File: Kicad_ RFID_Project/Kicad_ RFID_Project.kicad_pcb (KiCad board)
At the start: 2 copper layers, 75 x 75 mm, 34 parts, among them J1 Conn_01x08, J2 Conn_ST_STDC14, J3 10172013-00011LF, Q1 2N3904, SW1 RESET, U1 STM32L476RGTx, U2 AZ1117CH2-3.3

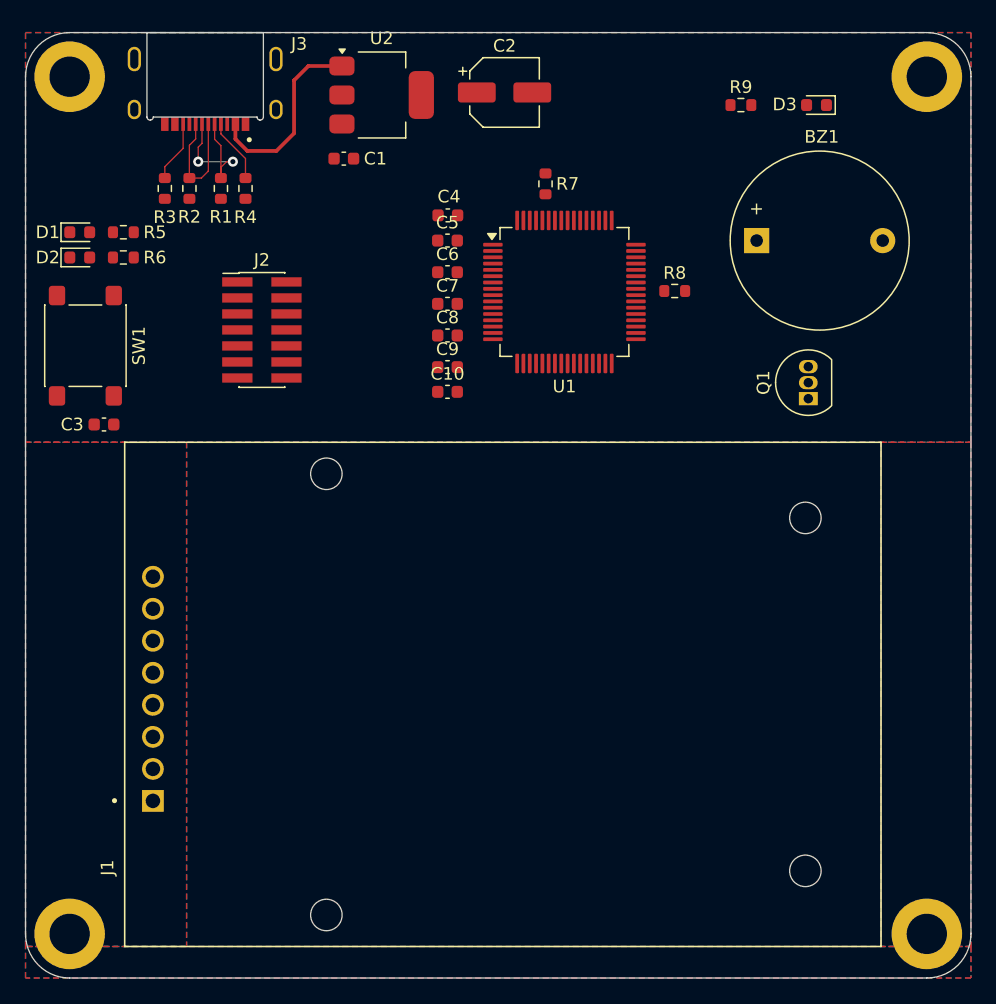
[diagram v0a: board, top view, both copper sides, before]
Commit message: ajout des leds electrostatiques pour l'USB-C
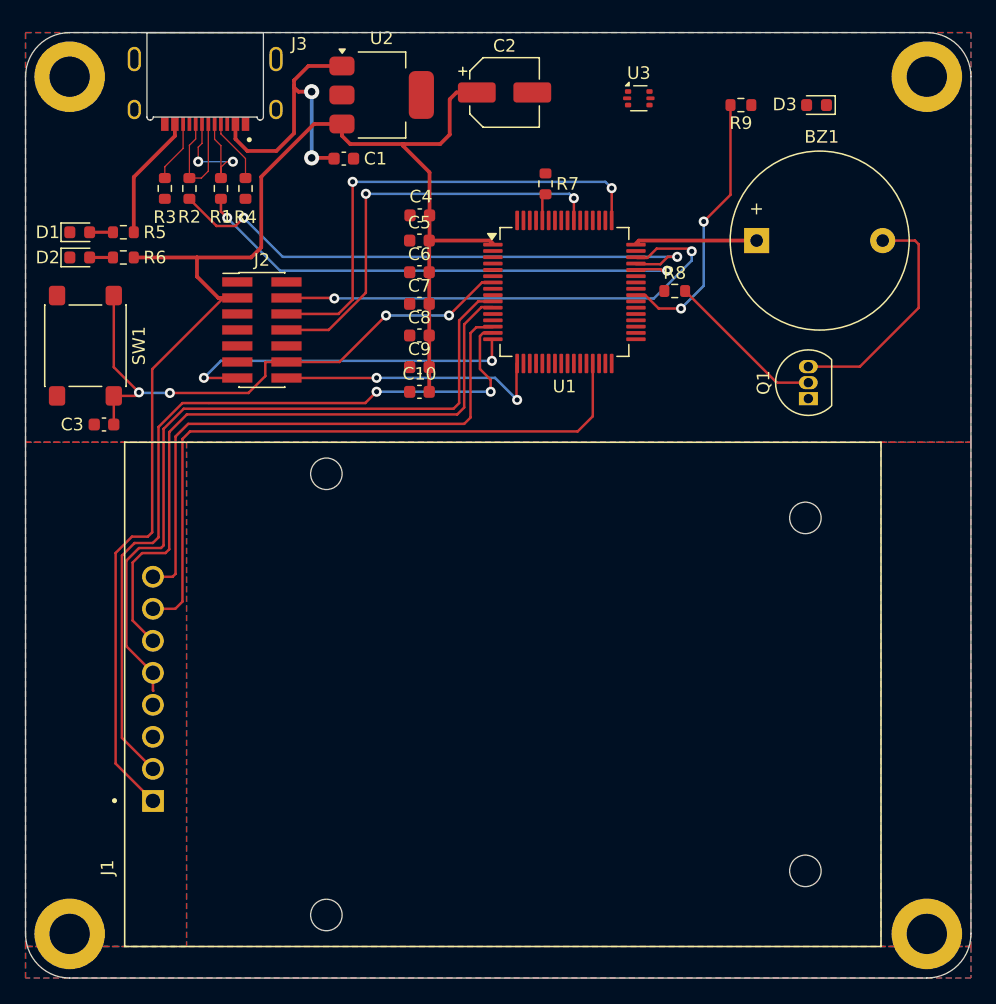
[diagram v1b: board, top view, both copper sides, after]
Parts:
- added U3: USBLC6-2P6, Package_TO_SOT_SMD:SOT-666, F.Cu at (157.4, 65.2)
- moved C10 2.22 mm to (140.0, 88.5)
- moved C4 2.22 mm to (140.0, 74.5)
- moved C5 2.22 mm to (140.0, 76.5)
- moved C6 2.22 mm to (140.0, 79.0)
- moved C7 2.22 mm to (140.0, 81.5)
- moved C8 2.22 mm to (140.0, 84.0)
- moved C9 2.22 mm to (140.0, 86.5)
- turned R9 to 180 degrees
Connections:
- R1 pad 1: D- -> Net-(R1-Pad1)
- R2 pad 2: D+ -> Net-(R2-Pad2)
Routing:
- net +3.3V: track 0.00 -> 126.7 mm
- net SPI2_RST: track 0.00 -> 63.6 mm, vias 0 -> 2
- net SPI2_MISO: track 0.00 -> 58.1 mm
- net SPI2_MOSI: track 0.00 -> 53.2 mm
- net SPI2_SCK: track 0.00 -> 53.0 mm
- net SPI2_SDA: track 0.00 -> 45.5 mm
- net NRST: track 0.00 -> 45.3 mm, vias 0 -> 4
- net USB_DP: track 0.00 -> 44.7 mm, vias 0 -> 2
- net USB_DM: track 0.00 -> 40.9 mm, vias 0 -> 2
- net SWDIO: track 0.00 -> 38.9 mm, vias 0 -> 2
- net SWCLK: track 0.00 -> 38.4 mm, vias 0 -> 2
- net SWO: track 0.00 -> 33.8 mm, vias 0 -> 2
- net USART2_TX: track 0.00 -> 27.8 mm, vias 0 -> 2
- net USART2_RX: track 0.00 -> 21.9 mm, vias 0 -> 2
- net USER_LED: track 0.00 -> 21.8 mm, vias 0 -> 2
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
